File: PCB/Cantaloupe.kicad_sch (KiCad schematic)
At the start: 127 parts, among them J1 OLED, J2 Trackpad, J3 USB_In, J4 Split_comm_link, J5 RGB_Out, J6 SWD, Q1 AO3400, Q2 AO3400, SW1 MX, SW10 MX, SW11 MX, SW12 MX, SW13 MX, SW14 MX, SW15 MX, SW16 MX, SW17 MX, SW18 MX, SW19 MX, SW2 MX, SW20 MX, SW21 MX, SW22 MX, SW23 MX, SW24 MX, SW25 MX, SW26 MX, SW27 MX, SW28 MX, SW29 MX, SW3 MX, SW30 MX, SW31 Encoder, SW32 Reset, SW4 MX, SW5 MX, SW6 MX, SW7 MX, SW8 MX, SW9 MX, U1 STM32F4x1CxUx, U2 XC6206P332MR, U3 SRV05-4, U4 SRV05-4, Y1 8MHz

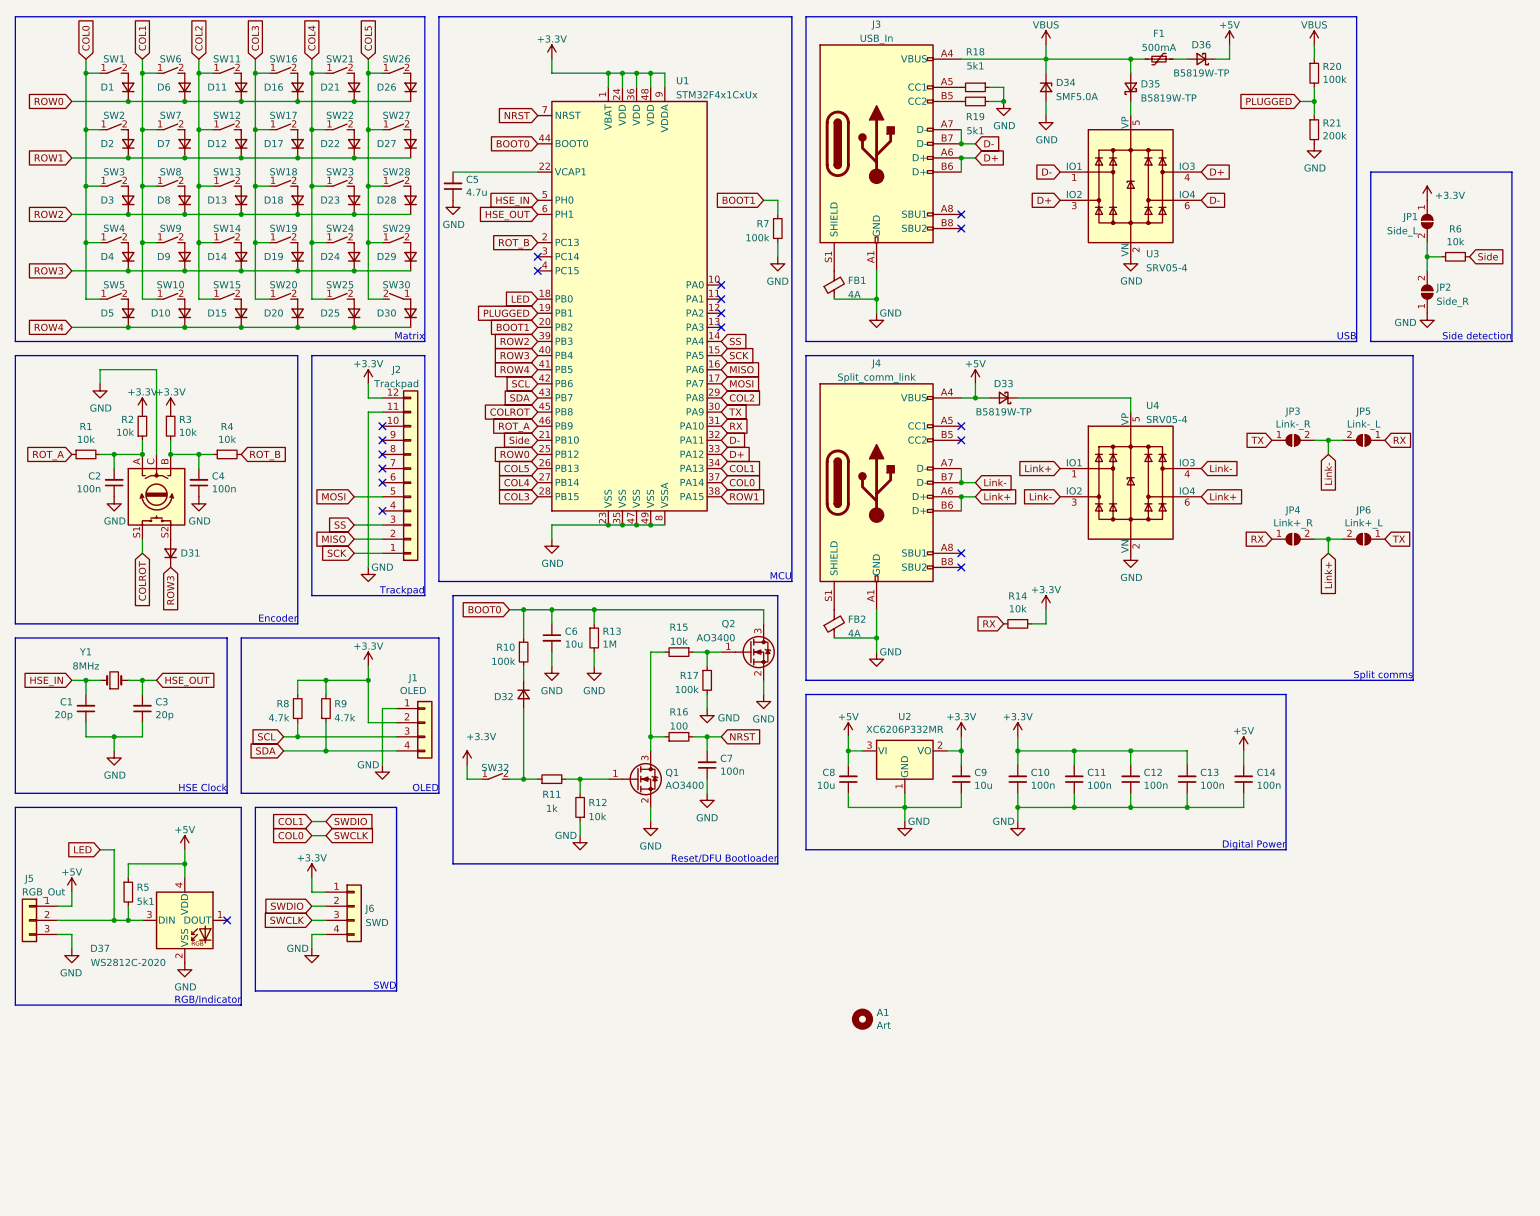
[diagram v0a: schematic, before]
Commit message: Further refinements to V2.1
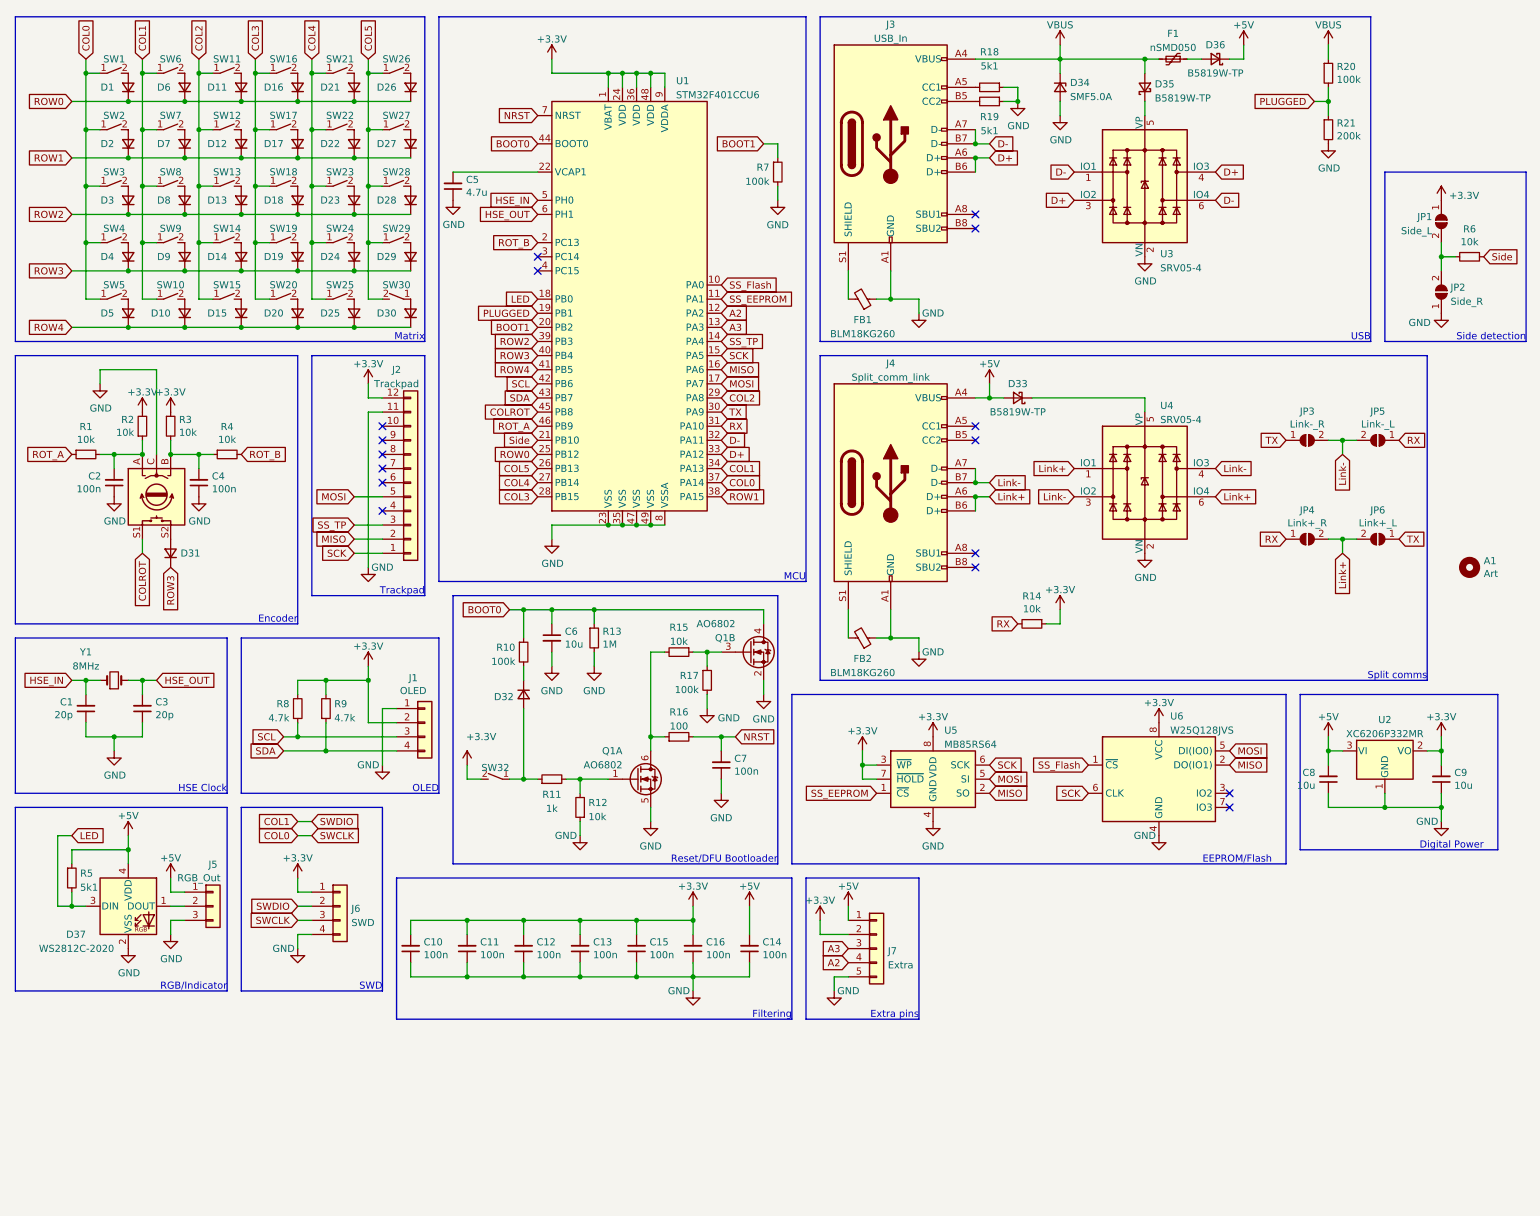
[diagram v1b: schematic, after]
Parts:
- removed Q1, Q2: AO3400, Package_TO_SOT_SMD:SOT-23, symbol Transistor_FET:2N7002
- added C15, C16: 100n, Capacitor_SMD:C_0603_1608Metric, symbol Device:C_Small
- added J7: Extra, Ariamelon:PinHeader_1x05_P2.54mm_Vertical_Silkless, symbol Connector_Generic:Conn_01x05
- added Q1: AO6802, Package_TO_SOT_SMD:SOT-23-6, symbol Device:Q_Dual_NMOS_G1S2G2D2S1D1
- added U5: MB85RS64, Package_SO:SSOP-8_3.9x5.05mm_P1.27mm, symbol Memory_NVRAM:MB85RS64
- added U6: W25Q128JVS, Package_SO:SOIC-8_5.275x5.275mm_P1.27mm, symbol Memory_Flash:W25Q128JVS
- A1, J1, J5, JP1, JP2, JP3, JP4, JP5, JP6: now left out of the parts list
- C1, C3: LCSC part number (none) -> C1648
- C10, C11, C12, C13, C14, C2, C4, C7: LCSC part number (none) -> C14663
- C5: LCSC part number (none) -> C19666
- C6, C8, C9: LCSC part number (none) -> C19702
- D1, D10, D11, D12, D13, D14, D15, D16, D17, D18, D19, D2, D20, D21, D22, D23, D24, D25, D26, D27, D28, D29, D3, D30, D31, D32, D4, D5, D6, D7, D8, D9: LCSC part number (none) -> C81598
- D33, D35, D36: LCSC part number (none) -> C8598
- D34: LCSC part number (none) -> C193402
- D37: LCSC part number (none) -> C965556
- F1: value 500mA -> nSMD050; LCSC C69688 -> (none); LCSC part number (none) -> C69688
- FB1, FB2: value 4A -> BLM18KG260; LCSC C2847222 -> (none); LCSC part number (none) -> C88981
- J3, J4: LCSC C168688 -> (none); LCSC part number (none) -> C168688
- J6: footprint Ariamelon:Debug_SWD -> Ariamelon:PinHeader_1x04_P2.54mm_Vertical_SIlkless; now left out of the parts list
- R1, R12, R14, R15, R2, R3, R4, R6: LCSC part number (none) -> C25804
- R10, R17, R20, R7: LCSC part number (none) -> C25803
- R11: LCSC part number (none) -> C21190
- R13: LCSC part number (none) -> C22935
- R16: LCSC part number (none) -> C22775
- R18, R19, R5: LCSC part number (none) -> C23186
- R21: LCSC part number (none) -> C25811
- R8, R9: LCSC part number (none) -> C23162
- SW31: LCSC part number (none) -> C470748
- SW32: footprint Ariamelon:Switch_TS24CA_Flippable -> Ariamelon:Switch_TS24ZJ_Flippable; LCSC part number (none) -> C398056
- U1: value STM32F4x1CxUx -> STM32F401CCU6; LCSC part number (none) -> C79861
- U2: LCSC part number (none) -> C5446
- U3, U4: LCSC part number (none) -> C85364
- Y1: LCSC part number (none) -> C115962
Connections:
- net +3V3: now also SW32.2 (B), C15.2, C16.2, J7.2 (Pin_2), U5.3 (~{WP}), U5.7 (~{HOLD}), U5.8 (VDD), U6.8 (VCC); no longer SW32.1 (A)
- net +5V: now also J7.1 (Pin_1)
- net BOOT0: now also Q1.4 (D)
- net GND: now also C15.1, C16.1, J7.5 (Pin_5), Q1.2 (S), Q1.5 (S), U5.4 (GND), U6.4 (GND)
- net LED: no longer J5.2 (Pin_2)
- net MISO: now also U5.2 (SO), U6.2 (DO(IO1))
- net MOSI: now also U5.5 (SI), U6.5 (DI(IO0))
- net SCK: now also U5.6 (SCK), U6.6 (CLK)
- net SS_Flash: now reaches U1.10 (PA0)
- net SS_Flash: now also U6.1 (~{CS})
- net SS_EEPROM: now reaches U1.11 (PA1)
- net SS_EEPROM: now also U5.1 (~{CS})
- net A2: now reaches U1.12 (PA2)
- net A2: now also J7.4 (Pin_4)
- net A3: now reaches U1.13 (PA3)
- net A3: now also J7.3 (Pin_3)
- net at D32.2 (A), R11.1: now also SW32.1 (A); no longer SW32.2 (B)
- net at R11.2, R12.2: now also Q1.1 (G)
- net at R15.2, R16.1: now also Q1.6 (D)
- net at R15.1, R17.1: now also Q1.3 (G)
- net at D37.1 (DOUT): now also J5.2 (Pin_2)
- net SS renamed SS_TP
- no-connect marks 19 -> 16
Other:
- note added: "EEPROM/Flash"
- note added: "Extra pins"
- note added: "Filtering"
- moved on the sheet: A1, C10, C11, C12, C13, C14, C7, C8, C9, D33, D34, D35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

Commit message: Further updates to V2.1
Fixed mistakes with bottom cases. Added piece which is meant to mate with the button, allowing the reset to be pressed without needing a screwdriver. Update to USB port name and footprint (no functional change). Updated pin assignments. Rerouted board.
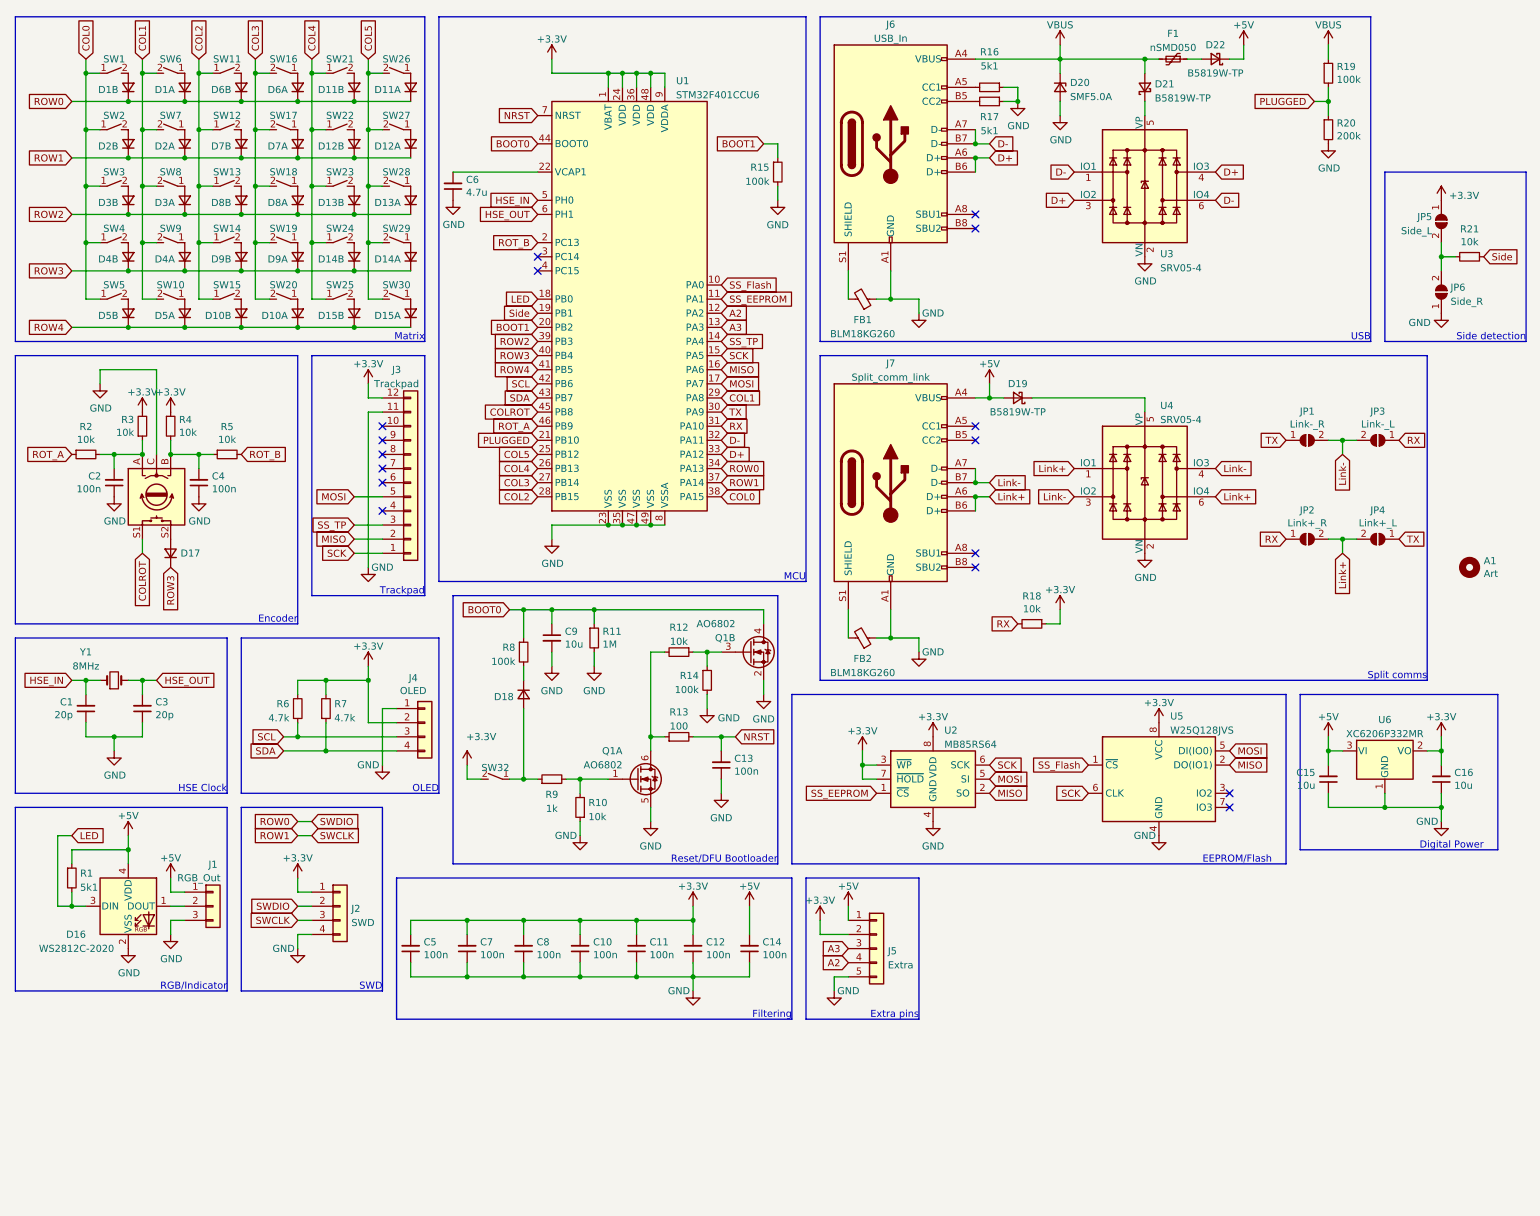
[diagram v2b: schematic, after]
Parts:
- removed D1, D10, D11, D12, D13, D14, D15, D16, D17, D18, D19, D2, D20, D21, D22, D23, D24, D25, D26, D27, D28, D29, D3, D30, D4, D5, D6, D7, D8, D9: D, Ariamelon:D_SOD-123, symbol Device:D_Small
- removed J7: Extra, Ariamelon:PinHeader_1x05_P2.54mm_Vertical_Silkless, symbol Connector_Generic:Conn_01x05
- added D1, D10, D11, D12, D13, D14, D15, D2, D3, D4, D5, D6, D7, D8, D9: D_Dual_CommonCathode_AAK_Split_Small, Package_TO_SOT_SMD:SOT-23, symbol Ariamelon:D_Dual_CommonCathode_AAK_Split_Small
- added J5: Extra, Ariamelon:PinHeader_1x05_P2.54mm_Vertical_Silkless, symbol Connector_Generic:Conn_01x05
- FB1, FB2: footprint Inductor_SMD:L_0805_2012Metric -> Inductor_SMD:L_0603_1608Metric
- J3: renamed from J2; LCSC part number (none) -> C88360
- J6: renamed from J3; footprint Ariamelon:USB-C-C168688 -> Ariamelon:HRO-TYPE-C-31-M-13x
- J7: renamed from J4; footprint Ariamelon:USB-C-C168688 -> Ariamelon:HRO-TYPE-C-31-M-13x
- SW1, SW10, SW11, SW12, SW13, SW14, SW15, SW16, SW17, SW18, SW19, SW2, SW20, SW21, SW22, SW23, SW24, SW25, SW26, SW27, SW28, SW29, SW3, SW30, SW4, SW5, SW6, SW7, SW8, SW9: now left out of the parts list
- U2: renamed from U5; LCSC part number (none) -> C8741
- U5: renamed from U6; LCSC part number (none) -> C97521
- renumbered C13 to C10, C15 to C11, C16 to C12, C7 to C13, C8 to C15, C9 to C16, C10 to C5, C5 to C6, C11 to C7, C12 to C8, C6 to C9, D37 to D16, D31 to D17, D32 to D18, D33 to D19, D34 to D20, D35 to D21, D36 to D22, J5 to J1, J6 to J2, J1 to J4, JP3 to JP1, JP4 to JP2, JP5 to JP3, JP6 to JP4, JP1 to JP5, JP2 to JP6, R5 to R1, R12 to R10, R13 to R11, R15 to R12, R16 to R13, R17 to R14, R7 to R15, R18 to R16, R19 to R17, R14 to R18, R20 to R19, R1 to R2, R21 to R20, R6 to R21, R2 to R3, R3 to R4, R4 to R5, R8 to R6, R9 to R7, R10 to R8, R11 to R9, U2 to U6
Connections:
- net +3V3: now also J5.2 (Pin_2)
- net +5V: now also J5.1 (Pin_1)
- net A2: now also J5.4 (Pin_4)
- net A3: now also J5.3 (Pin_3)
- net COL0: now also U1.38 (PA15); no longer J2.3 (Pin_3), U1.37 (PA14)
- net COL1: now also SW10.2 (B), SW6.2 (B), SW7.2 (B), SW8.2 (B), SW9.2 (B), U1.29 (PA8); no longer J2.2 (Pin_2), SW10.1 (A), SW6.1 (A), SW7.1 (A), SW8.1 (A), SW9.1 (A), U1.34 (PA13)
- net COL2: now also U1.28 (PB15); no longer U1.29 (PA8)
- net COL3: now also SW16.2 (B), SW17.2 (B), SW18.2 (B), SW19.2 (B), SW20.2 (B), U1.27 (PB14); no longer SW16.1 (A), SW17.1 (A), SW18.1 (A), SW19.1 (A), SW20.1 (A), U1.28 (PB15)
- net COL4: now also U1.26 (PB13); no longer U1.27 (PB14)
- net COL5: now also SW26.2 (B), SW27.2 (B), SW28.2 (B), SW29.2 (B), U1.25 (PB12); no longer SW26.1 (A), SW27.1 (A), SW28.1 (A), SW29.1 (A), U1.26 (PB13)
- net GND: now also J5.5 (Pin_5)
- net PLUGGED: now also U1.21 (PB10); no longer U1.19 (PB1)
- net ROW0: now also J2.2 (Pin_2), U1.34 (PA13), D1.3 (K), D1.3 (K), D11.3 (K), D11.3 (K), D6.3 (K), D6.3 (K); no longer U1.25 (PB12)
- net ROW1: now also J2.3 (Pin_3), U1.37 (PA14), D12.3 (K), D12.3 (K), D2.3 (K), D2.3 (K), D7.3 (K), D7.3 (K); no longer U1.38 (PA15)
- net ROW2: now also D13.3 (K), D13.3 (K), D3.3 (K), D3.3 (K), D8.3 (K), D8.3 (K)
- net ROW3: now also D14.3 (K), D14.3 (K), D4.3 (K), D4.3 (K), D9.3 (K), D9.3 (K)
- net ROW4: now also D10.3 (K), D10.3 (K), D15.3 (K), D15.3 (K), D5.3 (K), D5.3 (K)
- net Side: now also U1.19 (PB1); no longer U1.21 (PB10)
- net at SW1.2 (B): now also D1.2 (A)
- net at SW2.2 (B): now also D2.2 (A)
- net at SW3.2 (B): now also D3.2 (A)
- net at SW4.2 (B): now also D4.2 (A)
- net at SW5.2 (B): now also D5.2 (A)
- net at SW11.2 (B): now also D6.2 (A)
- net at SW12.2 (B): now also D7.2 (A)
- net at SW13.2 (B): now also D8.2 (A)
- net at SW14.2 (B): now also D9.2 (A)
- net at SW15.2 (B): now also D10.2 (A)
- net at SW21.2 (B): now also D11.2 (A)
- net at SW22.2 (B): now also D12.2 (A)
- net at SW23.2 (B): now also D13.2 (A)
- net at SW24.2 (B): now also D14.2 (A)
- net at SW25.2 (B): now also D15.2 (A)
- net at SW30.1 (A): now also D15.1 (A)
- new net: D1.1 (A), SW6.1 (A)
- new net: D2.1 (A), SW7.1 (A)
- new net: D3.1 (A), SW8.1 (A)
- new net: D4.1 (A), SW9.1 (A)
- new net: D5.1 (A), SW10.1 (A)
- new net: D6.1 (A), SW16.1 (A)
- new net: D7.1 (A), SW17.1 (A)
- new net: D8.1 (A), SW18.1 (A)
- new net: D9.1 (A), SW19.1 (A)
- new net: D10.1 (A), SW20.1 (A)
- new net: D11.1 (A), SW26.1 (A)
- new net: D12.1 (A), SW27.1 (A)
- new net: D13.1 (A), SW28.1 (A)
- new net: D14.1 (A), SW29.1 (A)

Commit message: Added another 10u filtering cap. Rerouted power track. Changed pin assignments. Changed values of VBUS detect to use already existing values on the board.
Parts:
- added C17: 10u, Capacitor_SMD:C_0603_1608Metric, symbol Device:C_Small
- D17, D18: LCSC (none) -> SOD-123 diode"
- J1: LCSC (none) -> USB C 2.0 jack"
- J6, J7: LCSC (none) -> USB C 2.0 jack"; LCSC part number C168688 -> C2848620
- R19: value 100k -> 5.1k
- R20: value 200k -> 10k
- R6, R7: value 4.7k -> 4k7
- U3, U4, U5: LCSC (none) -> "
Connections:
- net +3V3: now also C17.2
- net COL0: now also J2.3 (Pin_3), U1.37 (PA14); no longer U1.38 (PA15)
- net GND: now also C17.1
- net ROW1: now also U1.38 (PA15); no longer J2.3 (Pin_3), U1.37 (PA14)
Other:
- moved on the sheet: C15, C16, U6
